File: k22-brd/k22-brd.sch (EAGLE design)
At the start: 28 parts, among them IC1 LMS8117, J1 61302011121, J2 61302011121, J3 CORTEX_DEBUG_PTH, SW1 KMR731NGLFS

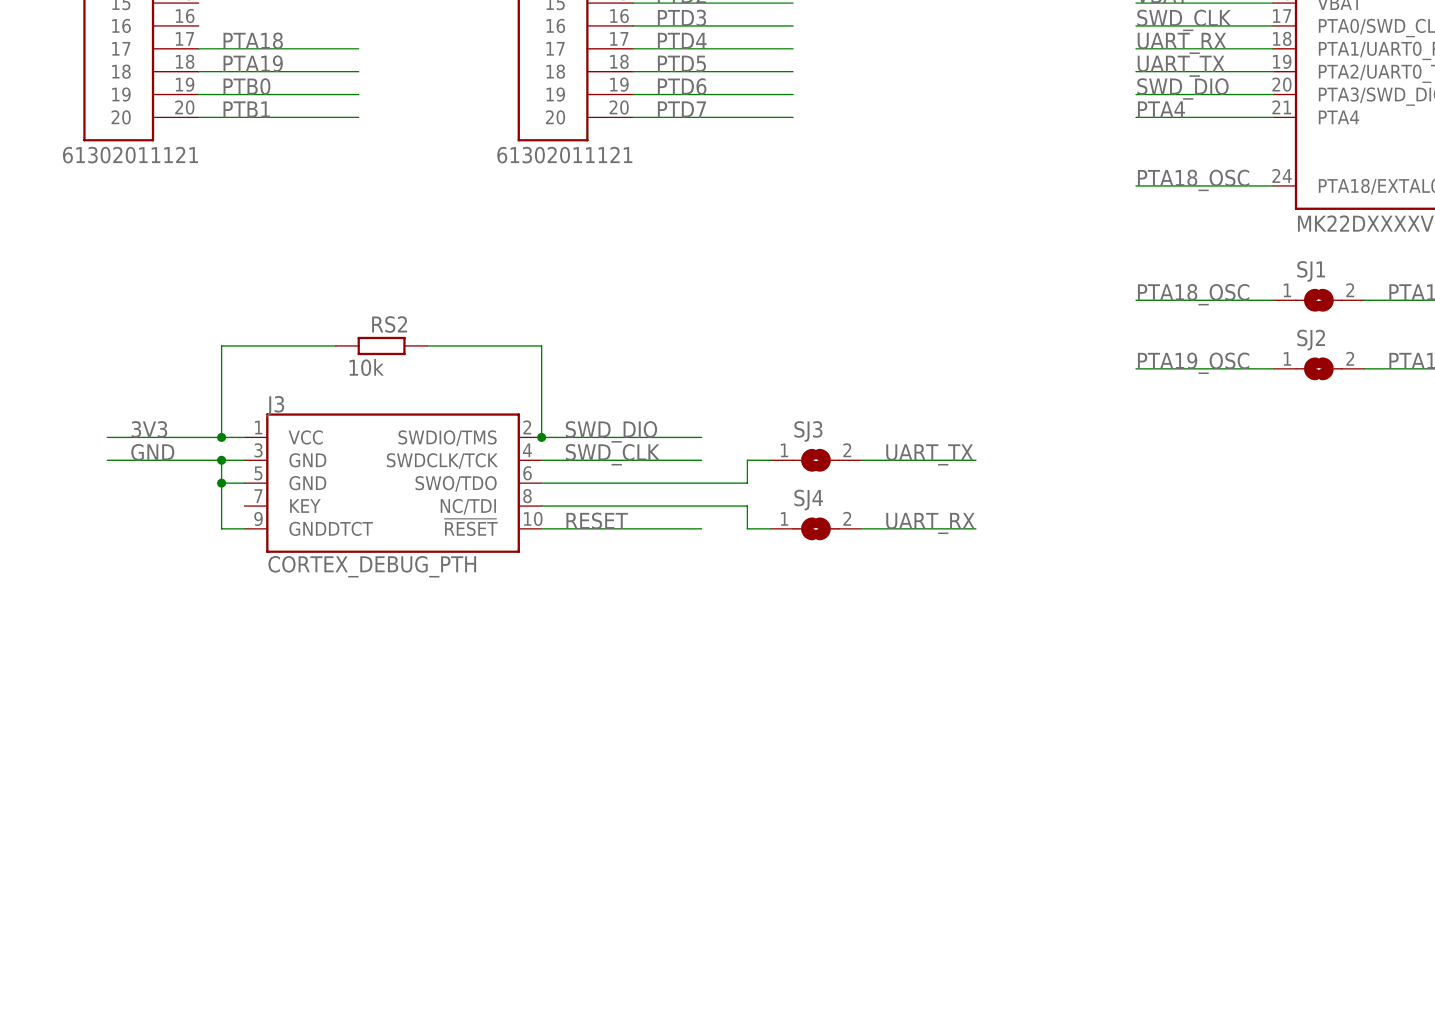
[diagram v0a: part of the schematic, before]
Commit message: Added lib for ESD and Crystal and added those into brd schematic
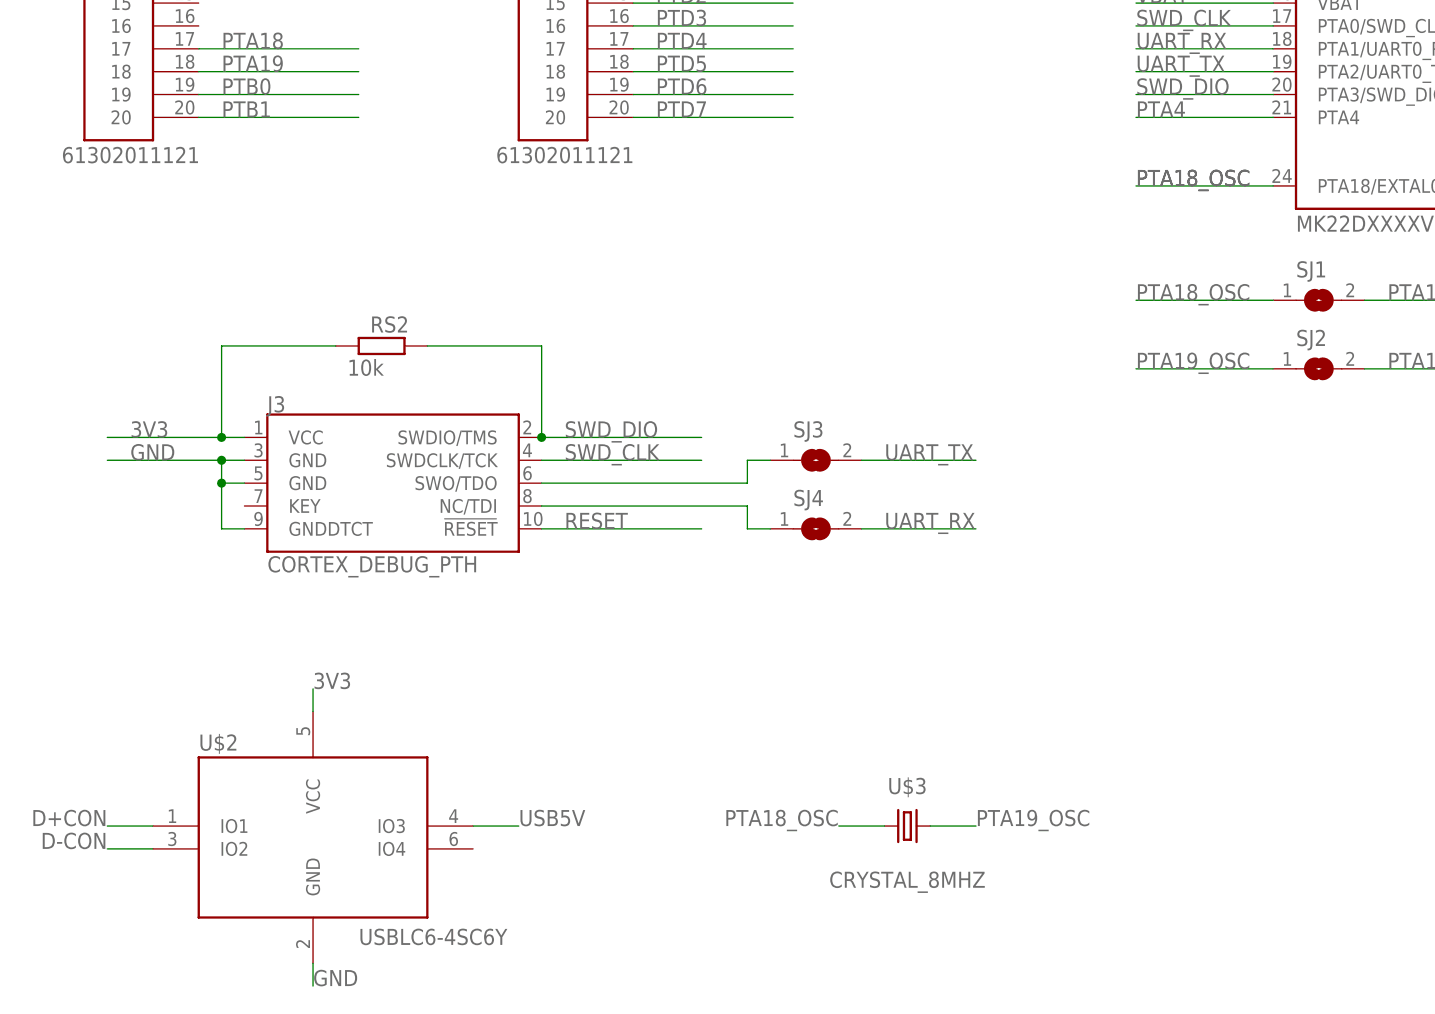
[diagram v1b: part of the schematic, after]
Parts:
- added U$2: USBLC6-4SC6Y, vym0038_k22_misc:USBLC6-4SC6Y
- added U$3: CRYSTAL_8MHZ, vym0038_k22_misc:CRYSTAL_8MHZ
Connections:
- net 3V3: now also U$2.VCC
- net D+CON: now also U$2.IO1
- net D-CON: now also U$2.IO2
- net GND: now also U$2.GND
- net PTA18_OSC: now also U$3.1
- net PTA19_OSC: now also U$3.2
- net USB5V: now also U$2.IO3
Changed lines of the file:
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@@
 <layers>
 <layer number="1" name="Top" color="4" fill="1" visible="no" active="no"/>
+<layer number="2" name="Route2" color="16" fill="1" visible="no" active="no"/>
+<layer number="3" name="Route3" color="17" fill="1" visible="no" active="no"/>
+<layer number="4" name="Route4" color="18" fill="1" visible="no" active="no"/>
+<layer number="5" name="Route5" color="19" fill="1" visible="no" active="no"/>
+<layer number="6" name="Route6" color="25" fill="1" visible="no" active="no"/>
+<layer number="7" name="Route7" color="26" fill="1" visible="no" active="no"/>
+<layer number="8" name="Route8" color="27" fill="1" visible="no" active="no"/>
+<layer number="9" name="Route9" color="28" fill="1" visible="no" active="no"/>
+<layer number="10" name="Route10" color="29" fill="1" visible="no" active="no"/>
+<layer number="11" name="Route11" color="30" fill="1" visible="no" active="no"/>
+<layer number="12" name="Route12" color="20" fill="1" visible="no" active="no"/>
+<layer number="13" name="Route13" color="21" fill="1" visible="no" active="no"/>
+<layer number="14" name="Route14" color="22" fill="1" visible="no" active="no"/>
+<layer number="15" name="Route15" color="23" fill="1" visible="no" active="no"/>
 <layer number="16" name="Bottom" color="1" fill="1" visible="no" active="no"/>
 <layer number="17" name="Pads" color="2" fill="1" visible="no" active="no"/>
@@
 <layer number="115" name="ReferenceISLANDS" color="7" fill="1" visible="yes" active="yes"/>
 <layer number="116" name="Patch_BOT" color="7" fill="4" visible="yes" active="yes"/>
+<layer number="117" name="Outline-717" color="10" fill="1" visible="no" active="no"/>
 <layer number="118" name="Rect_Pads" color="7" fill="1" visible="yes" active="yes"/>
+<layer number="119" name="TODO" color="38" fill="1" visible="no" active="no"/>
+<layer number="120" name="_Dimension" color="7" fill="1" visible="no" active="no"/>
 <layer number="121" name="_tsilk" color="7" fill="1" visible="yes" active="yes"/>
 <layer number="122" name="_bsilk" color="7" fill="1" visible="yes" active="yes"/>
@@
 <layer number="128" name="_bValues" color="7" fill="1" visible="yes" active="yes"/>
 <layer number="129" name="Mask" color="7" fill="1" visible="yes" active="yes"/>
+<layer number="130" name="SMDSTROOK" color="7" fill="1" visible="no" active="no"/>
 <layer number="131" name="tAdjust" color="7" fill="1" visible="yes" active="yes"/>
 <layer number="132" name="bAdjust" color="7" fill="1" visible="yes" active="yes"/>
+<layer number="133" name="bottom_silk" color="7" fill="1" visible="no" active="no"/>
+<layer number="134" name="mbFinish" color="7" fill="1" visible="no" active="no"/>
+<layer number="135" name="_tanames" color="7" fill="1" visible="no" active="no"/>
+<layer number="136" name="_banames" color="7" fill="1" visible="no" active="no"/>
+<layer number="137" name="_taDocu" color="7" fill="1" visible="no" active="no"/>
+<layer number="138" name="_baDocu" color="7" fill="1" visible="no" active="no"/>
+<layer number="139" name="mtKeepout" color="7" fill="1" visible="no" active="no"/>
+<layer number="140" name="mbKeepout" color="7" fill="1" visible="no" active="no"/>
+<layer number="141" name="mtRestrict" color="7" fill="1" visible="no" active="no"/>
+<layer number="142" name="mbRestrict" color="7" fill="1" visible="no" active="no"/>
+<layer number="143" name="mvRestrict" color="7" fill="1" visible="no" active="no"/>
 <layer number="144" name="Drill_legend" color="7" fill="1" visible="yes" active="yes"/>
 <layer number="145" name="DrillLegend_01-16" color="2" fill="9" visible="no" active="yes"/>
 <layer number="146" name="DrillLegend_01-20" color="3" fill="9" visible="no" active="yes"/>
+<layer number="147" name="mMeasures" color="7" fill="1" visible="no" active="no"/>
+<layer number="148" name="mDocument" color="7" fill="1" visible="no" active="no"/>
+<layer number="149" name="mReference" color="7" fill="1" visible="no" active="no"/>
 <layer number="150" name="Notes" color="7" fill="1" visible="yes" active="yes"/>
 <layer number="151" name="HeatSink" color="7" fill="1" visible="yes" active="yes"/>
@@
 <layer number="154" name="FabDoc2" color="7" fill="1" visible="yes" active="yes"/>
 <layer number="155" name="FabDoc3" color="7" fill="1" visible="yes" active="yes"/>
+<layer number="166" name="AntennaArea" color="7" fill="1" visible="no" active="no"/>
+<layer number="168" name="4mmHeightArea" color="7" fill="1" visible="no" active="no"/>
+<layer number="191" name="mNets" color="7" fill="1" visible="no" active="no"/>
+<layer number="192" name="mBusses" color="7" fill="1" visible="no" active="no"/>
+<layer number="193" name="mPins" color="7" fill="1" visible="no" active="no"/>
+<layer number="194" name="mSymbols" color="7" fill="1" visible="no" active="no"/>
+<layer number="195" name="mNames" color="7" fill="1" visible="no" active="no"/>
+<layer number="196" name="mValues" color="7" fill="1" visible="no" active="no"/>
 <layer number="199" name="Contour" color="7" fill="1" visible="yes" active="yes"/>
 <layer number="200" name="200bmp" color="7" fill="10" visible="yes" active="yes"/>
@@
 <layer number="250" name="Descript" color="7" fill="1" visible="yes" active="yes"/>
 <layer number="251" name="SMDround" color="7" fill="1" visible="yes" active="yes"/>
+<layer number="253" name="Extra" color="7" fill="1" visible="no" active="no"/>
 <layer number="254" name="cooling" color="7" fill="1" visible="yes" active="yes"/>
 <layer number="255" name="routoute" color="7" fill="1" visible="yes" active="yes"/>
@@
 <part name="SJ3" library="jumper" library_urn="urn:adsk.eagle:library:252" deviceset="SJ" device="" package3d_urn="urn:adsk.eagle:package:15471/1"/>
 <part name="SJ4" library="jumper" library_urn="urn:adsk.eagle:library:252" deviceset="SJ" device="" package3d_urn="urn:adsk.eagle:package:15471/1"/>
+<part name="U$2" library="vym0038_k22_misc" deviceset="USBLC6-4SC6Y" device=""/>
+<part name="U$3" library="vym0038_k22_misc" deviceset="CRYSTAL_8MHZ" device=""/>
 </parts>
 <sheets>
@@
 <attribute name="VALUE" x="25.4" y="-6.35" size="1.778" layer="96"/>
 </instance>
+<instance part="U$2" gate="G$1" x="-27.94" y="-38.1" smashed="yes">
+<attribute name="NAME" x="-40.64" y="-27.178" size="1.778" layer="95"/>
+<attribute name="VALUE" x="-22.86" y="-48.768" size="1.778" layer="96"/>
+</instance>
+<instance part="U$3" gate="G$1" x="38.1" y="-35.56" smashed="yes">
+<attribute name="NAME" x="38.1" y="-32.004" size="1.778" layer="95" align="bottom-center"/>
+<attribute name="VALUE" x="38.1" y="-40.64" size="1.778" layer="96" align="top-center"/>
+</instance>
 </instances>
 <busses>
@@
 <label x="-48.26" y="5.08" size="1.778" layer="95"/>
 </segment>
+<segment>
+<wire x1="-27.94" y1="-50.8" x2="-27.94" y2="-53.34" width="0.1524" layer="91"/>
+<pinref part="U$2" gate="G$1" pin="GND"/>
+<label x="-27.94" y="-53.34" size="1.778" layer="95"/>
+</segment>
 </net>
 <net name="VBUSCON" class="0">
@@
 <label x="226.06" y="66.04" size="1.778" layer="95"/>
 </segment>
+<segment>
+<wire x1="-50.8" y1="-35.56" x2="-45.72" y2="-35.56" width="0.1524" layer="91"/>
+<pinref part="U$2" gate="G$1" pin="IO1"/>
+<label x="-50.8" y="-35.56" size="1.778" layer="95" rot="MR0"/>
+</segment>
 </net>
 <net name="USBGNDSHIELD" class="0">
@@
 <label x="226.06" y="58.42" size="1.778" layer="95"/>
 </segment>
+<segment>
+<wire x1="-50.8" y1="-38.1" x2="-45.72" y2="-38.1" width="0.1524" layer="91"/>
+<pinref part="U$2" gate="G$1" pin="IO2"/>
+<label x="-50.8" y="-38.1" size="1.778" layer="95" rot="MR0"/>
+</segment>
 </net>
 <net name="CC2CON" class="0">
@@
 <wire x1="-40.64" y1="137.16" x2="-48.26" y2="137.16" width="0.1524" layer="91"/>
 <label x="-50.8" y="137.16" size="1.778" layer="95"/>
+</segment>
+<segment>
+<wire x1="-5.08" y1="-35.56" x2="-10.16" y2="-35.56" width="0.1524" layer="91"/>
+<pinref part="U$2" gate="G$1" pin="IO3"/>
+<label x="-5.08" y="-35.56" size="1.778" layer="95"/>
 </segment>
 </net>
@@
 <wire x1="63.5" y1="35.56" x2="78.74" y2="35.56" width="0.1524" layer="91"/>
 <label x="63.5" y="35.56" size="1.778" layer="95"/>
+<label x="63.5" y="35.56" size="1.778" layer="95"/>
 </segment>
 <segment>
@@
 <label x="63.5" y="22.86" size="1.778" layer="95"/>
 </segment>
+<segment>
+<pinref part="U$3" gate="G$1" pin="1"/>
+<wire x1="35.56" y1="-35.56" x2="30.48" y2="-35.56" width="0.1524" layer="91"/>
+<label x="30.48" y="-35.56" size="1.778" layer="95" rot="MR0"/>
+</segment>
 </net>
 <net name="PTA19_OSC" class="0">
@@
 <wire x1="63.5" y1="15.24" x2="78.74" y2="15.24" width="0.1524" layer="91"/>
 <label x="63.5" y="15.24" size="1.778" layer="95"/>
+</segment>
+<segment>
+<pinref part="U$3" gate="G$1" pin="2"/>
+<wire x1="40.64" y1="-35.56" x2="45.72" y2="-35.56" width="0.1524" layer="91"/>
+<label x="45.72" y="-35.56" size="1.778" layer="95"/>
 </segment>
 </net>
@@
 <junction x="-38.1" y="7.62"/>
 </segment>
-</net>
+<segment>
+<wire x1="-27.94" y1="-20.32" x2="-27.94" y2="-22.86" width="0.1524" layer="91"/>
+<pinref part="U$2" gate="G$1" pin="VCC"/>
+<label x="-27.94" y="-20.32" size="1.778" layer="95"/>
+</segment>
+</net>

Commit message: schema is done
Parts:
- removed SW1: KMR731NGLFS, Switch:KMR731NGLFS
- removed U$2: USBLC6-4SC6Y, vym0038_k22_misc:USBLC6-4SC6Y
- added CM4: 2u2, rcl:C-EUC0805
- added LED_3V3: (no value), led:LEDCHIP-LED0805
- added RV1: 1k, rcl:R-EU_M0805
- added SWB, SWR: KMR731NGLFS, Switch:KMR731NGLFS
- added U$4: USBLC6-2SC6, vym0038_k22_misc:USBLC6-2SC6
- CM3: value 2u2 -> 1u
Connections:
- new net N$2: LED_3V3.C, RV1.1
- net 3V3: now also LED_3V3.A, RR1.1; no longer U$2.VCC
- net D+CON: now also U$4.IO1; no longer U$2.IO1
- net D-CON: now also U$4.IO2; no longer U$2.IO2
- net GND: now also CM4.1, RV1.2, SWB.4, SWR.4, U$4.GND; no longer SW1.4, U$2.GND
- net PTA4: now also J1.16
- net PTD4: now also SWB.1
- net RESET: now also SWR.1; no longer SW1.1
- net USB5V: now also U$4.VUSB; no longer U$2.IO3
- net V3V: now also CM3.2
- net VOUT33: now also CM4.2; no longer CM3.2
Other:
- note added: "B BUTTON PTD4"
- moved on the sheet: CM3, CV1, CV2, DV1, DV2, IC1, J1, J2, J3, LED_PTD5, LU1, LU2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

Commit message: board created
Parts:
- renumbered SJ1 to SJM1, SJ2 to SJM2, SJ3 to SJS1, SJ4 to SJS2

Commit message: Basic routing done
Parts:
- removed IC1: LMS8117, IC_Power-Management:LD1117_SOT223
- added U$2: LMS8117AMP-3.3, vym0038_k22_misc:LMS8117AMP-3.3
- U$4: value USBLC6-2SC6 -> USBLC6-4SC6Y; device vym0038_k22_misc:USBLC6-2SC6 -> vym0038_k22_misc:USBLC6-4SC6Y
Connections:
- removed net V3V: CM1.2, CM2.2, CM3.2
- new net N$5: J1.4
- net 3V3: now also CM1.2, CM2.2, CM3.2, J1.5, U$2.VOUT; no longer IC1.VO
- net DM0: now also J1.9
- net DP0: now also J1.8
- net GND: now also J1.1, J1.10, J1.6, U$2.GND; no longer IC1.GND
- net PTD4: now also SWB.3; no longer SWB.1
- net RESET: now also J1.7
- net SWD_CLK: now also J1.12
- net SWD_DIO: now also J1.15
- net UART_RX: now also J1.14
- net UART_TX: now also J1.13
- net USB5V: now also J1.3
- net VI: now also U$2.VIN; no longer IC1.VI
- net VIN: now also J1.2
- net VREF: now also J1.11
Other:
- moved on the sheet: CV1, CV2, DV1, DV2, LED_3V3, RV1
